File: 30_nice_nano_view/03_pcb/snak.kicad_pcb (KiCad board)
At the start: 2 copper layers, 114 x 99 mm, 114 parts

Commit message: update
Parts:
- removed the REF** at (166.2, 79.5)
- removed the REF** at (166.2, 62.0)
- removed the REF** at (197.5, 123.0)
- removed the REF** at (94.8, 84.0)
- removed the REF** at (94.8, 66.5)
- removed the REF** at (113.2, 90.2)
- removed the REF** at (113.2, 72.8)
- removed the REF** at (113.2, 55.2)
- removed the REF** at (131.8, 84.2)
- removed the REF** at (131.8, 66.8)
- removed the REF** at (131.8, 49.2)
- removed the REF** at (150.2, 91.5)
- removed the REF** at (150.2, 74.0)
- removed the REF** at (150.2, 56.5)
- removed the REF** at (168.8, 84.2)
- removed the REF** at (168.8, 66.7)
- removed the REF** at (165.2, 114.8)
- removed the REF** at (193.1, 126.1)
- removed the REF** at (100.0, 85.0)
- removed the REF** at (100.0, 67.5)
- removed the REF** at (118.5, 91.2)
- removed the REF** at (118.5, 73.8)
- removed the REF** at (118.5, 56.2)
- removed the REF** at (137.0, 85.2)
- removed the REF** at (137.0, 67.8)
- removed the REF** at (137.0, 50.2)
- removed the REF** at (155.5, 92.5)
- removed the REF** at (155.5, 75.0)
- removed the REF** at (155.5, 57.5)
- removed the REF** at (174.0, 85.2)
- removed the REF** at (174.0, 67.7)
- removed the REF** at (170.0, 117.3)
- removed the REF** at (187.9, 124.6)
- removed the REF** at (100.0, 86.0)
- removed the REF** at (100.0, 68.5)
- removed the REF** at (118.5, 92.2)
- removed the REF** at (118.5, 74.8)
- removed the REF** at (118.5, 57.2)
- removed the REF** at (137.0, 86.2)
- removed the REF** at (137.0, 68.8)
- removed the REF** at (137.0, 51.2)
- removed the REF** at (155.5, 93.5)
- removed the REF** at (155.5, 76.0)
- removed the REF** at (155.5, 58.5)
- removed the REF** at (174.0, 86.2)
- removed the REF** at (174.0, 68.7)
- removed the REF** at (169.7, 118.3)
- removed the REF** at (187.5, 125.5)
- removed the REF** at (186.9, 94.1)
- removed the REF** at (186.1, 93.4)
- removed the REF** at (185.3, 92.6)
- removed the REF** at (193.7, 94.5)
- removed the REF** at (193.2, 58.0)
- removed the REF** at (196.4, 103.4)
- removed the REF** at (202.7, 103.4)
- added REF**: VIA-0.6mm, VIA-0.6mm, F.Cu at (166.2, 78.2)
- added REF**: VIA-0.6mm, VIA-0.6mm, F.Cu at (166.2, 60.7)
- added REF**: VIA-0.6mm, VIA-0.6mm, F.Cu at (183.6, 116.0)
- added REF**: VIA-0.6mm, VIA-0.6mm, F.Cu at (93.8, 84.0)
- added REF**: VIA-0.6mm, VIA-0.6mm, F.Cu at (93.8, 66.5)
- added REF**: VIA-0.6mm, VIA-0.6mm, F.Cu at (112.2, 90.2)
- added REF**: VIA-0.6mm, VIA-0.6mm, F.Cu at (112.2, 72.8)
- added REF**: VIA-0.6mm, VIA-0.6mm, F.Cu at (112.2, 55.2)
- added REF**: VIA-0.6mm, VIA-0.6mm, F.Cu at (130.8, 84.2)
- added REF**: VIA-0.6mm, VIA-0.6mm, F.Cu at (130.8, 66.8)
- added REF**: VIA-0.6mm, VIA-0.6mm, F.Cu at (130.8, 49.2)
- added REF**: VIA-0.6mm, VIA-0.6mm, F.Cu at (149.2, 91.5)
- added REF**: VIA-0.6mm, VIA-0.6mm, F.Cu at (149.2, 74.0)
- added REF**: VIA-0.6mm, VIA-0.6mm, F.Cu at (149.2, 56.5)
- added REF**: VIA-0.6mm, VIA-0.6mm, F.Cu at (167.8, 83.0)
- added REF**: VIA-0.6mm, VIA-0.6mm, F.Cu at (167.8, 65.5)
- added REF**: VIA-0.6mm, VIA-0.6mm, F.Cu at (164.3, 114.6)
- added REF**: VIA-0.6mm, VIA-0.6mm, F.Cu at (182.8, 120.9)
- added REF**: VIA-0.6mm, VIA-0.6mm, F.Cu at (106.2, 79.2)
- added REF**: VIA-0.6mm, VIA-0.6mm, F.Cu at (106.2, 61.8)
- added REF**: VIA-0.6mm, VIA-0.6mm, F.Cu at (124.8, 85.5)
- added REF**: VIA-0.6mm, VIA-0.6mm, F.Cu at (124.8, 68.0)
- added REF**: VIA-0.6mm, VIA-0.6mm, F.Cu at (124.8, 50.5)
- added REF**: VIA-0.6mm, VIA-0.6mm, F.Cu at (143.2, 79.5)
- added REF**: VIA-0.6mm, VIA-0.6mm, F.Cu at (143.2, 62.0)
- added REF**: VIA-0.6mm, VIA-0.6mm, F.Cu at (143.2, 44.5)
- added REF**: VIA-0.6mm, VIA-0.6mm, F.Cu at (161.8, 86.7)
- added REF**: VIA-0.6mm, VIA-0.6mm, F.Cu at (161.8, 69.2)
- added REF**: VIA-0.6mm, VIA-0.6mm, F.Cu at (161.8, 51.7)
- added REF**: VIA-0.6mm, VIA-0.6mm, F.Cu at (180.2, 78.2)
- added REF**: VIA-0.6mm, VIA-0.6mm, F.Cu at (180.2, 60.7)
- added REF**: VIA-0.6mm, VIA-0.6mm, F.Cu at (177.6, 113.7)
- added REF**: VIA-0.6mm, VIA-0.6mm, F.Cu at (100.0, 85.5)
- added REF**: VIA-0.6mm, VIA-0.6mm, F.Cu at (100.0, 68.0)
- added REF**: VIA-0.6mm, VIA-0.6mm, F.Cu at (118.5, 91.8)
- added REF**: VIA-0.6mm, VIA-0.6mm, F.Cu at (118.5, 74.2)
- added REF**: VIA-0.6mm, VIA-0.6mm, F.Cu at (118.5, 56.8)
- added REF**: VIA-0.6mm, VIA-0.6mm, F.Cu at (137.0, 85.8)
- added REF**: VIA-0.6mm, VIA-0.6mm, F.Cu at (137.0, 68.2)
- added REF**: VIA-0.6mm, VIA-0.6mm, F.Cu at (137.0, 50.8)
- added REF**: VIA-0.6mm, VIA-0.6mm, F.Cu at (155.5, 93.0)
- added REF**: VIA-0.6mm, VIA-0.6mm, F.Cu at (155.5, 75.5)
- added REF**: VIA-0.6mm, VIA-0.6mm, F.Cu at (155.5, 58.0)
- added REF**: VIA-0.6mm, VIA-0.6mm, F.Cu at (174.0, 84.5)
- added REF**: VIA-0.6mm, VIA-0.6mm, F.Cu at (174.0, 67.0)
- added REF**: VIA-0.6mm, VIA-0.6mm, F.Cu at (169.8, 117.8)
- added REF**: VIA-0.6mm, VIA-0.6mm, F.Cu at (187.7, 125.1)
- added REF**: VIA-0.6mm, VIA-0.6mm, F.Cu at (186.9, 92.8)
- added REF**: VIA-0.6mm, VIA-0.6mm, F.Cu at (186.1, 92.1)
- added REF**: VIA-0.6mm, VIA-0.6mm, F.Cu at (185.3, 91.3)
- added REF**: VIA-0.6mm, VIA-0.6mm, F.Cu at (193.7, 93.2)
- added REF**: VIA-0.6mm, VIA-0.6mm, F.Cu at (193.2, 56.7)
- added REF**: VIA-0.6mm, VIA-0.6mm, F.Cu at (196.4, 102.1)
- added REF**: VIA-0.6mm, VIA-0.6mm, F.Cu at (202.7, 102.1)
- moved D15 15.5 mm to (182.3, 118.7)
- moved H3 3.28 mm to (164.8, 71.4)
- moved H1 2.50 mm to (109.2, 61.1)
- moved H2 2.50 mm to (109.2, 78.7)
- moved D12 1.29 mm to (166.2, 81.2)
- moved D13 1.29 mm to (166.2, 63.7)
- moved DISP1 1.29 mm to (193.7, 79.7)
- moved JST1 1.29 mm to (200.3, 102.1)
- moved MCU1 1.29 mm to (193.7, 74.1)
- moved S12 1.29 mm to (174.0, 81.5)
- moved S13 1.29 mm to (174.0, 64.0)
- moved SW1 1.29 mm to (193.2, 57.8)
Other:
- outline, holes or cut-outs redrawn

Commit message: update
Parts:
- removed the REF** at (166.2, 78.2)
- removed the REF** at (166.2, 60.7)
- removed the REF** at (167.8, 83.0)
- removed the REF** at (167.8, 65.5)
- removed the REF** at (180.2, 78.2)
- removed the REF** at (180.2, 60.7)
- removed the REF** at (174.0, 84.5)
- removed the REF** at (174.0, 67.0)
- removed the REF** at (186.9, 92.8)
- removed the REF** at (186.1, 92.1)
- removed the REF** at (185.3, 91.3)
- removed the REF** at (193.7, 93.2)
- removed the REF** at (193.2, 56.7)
- removed the REF** at (196.4, 102.1)
- removed the REF** at (202.7, 102.1)
- added REF**: VIA-0.6mm, VIA-0.6mm, F.Cu at (166.2, 77.2)
- added REF**: VIA-0.6mm, VIA-0.6mm, F.Cu at (166.2, 59.7)
- added REF**: VIA-0.6mm, VIA-0.6mm, F.Cu at (167.8, 82.0)
- added REF**: VIA-0.6mm, VIA-0.6mm, F.Cu at (167.8, 64.5)
- added REF**: VIA-0.6mm, VIA-0.6mm, F.Cu at (180.2, 77.2)
- added REF**: VIA-0.6mm, VIA-0.6mm, F.Cu at (180.2, 59.7)
- added REF**: VIA-0.6mm, VIA-0.6mm, F.Cu at (174.0, 83.5)
- added REF**: VIA-0.6mm, VIA-0.6mm, F.Cu at (174.0, 66.0)
- added REF**: VIA-0.6mm, VIA-0.6mm, F.Cu at (186.9, 97.4)
- added REF**: VIA-0.6mm, VIA-0.6mm, F.Cu at (186.1, 96.7)
- added REF**: VIA-0.6mm, VIA-0.6mm, F.Cu at (185.3, 95.9)
- added REF**: VIA-0.6mm, VIA-0.6mm, F.Cu at (193.7, 97.8)
- added REF**: VIA-0.6mm, VIA-0.6mm, F.Cu at (193.2, 61.3)
- added REF**: VIA-0.6mm, VIA-0.6mm, F.Cu at (194.9, 106.5)
- added REF**: VIA-0.6mm, VIA-0.6mm, F.Cu at (201.2, 106.5)
- moved JST1 4.56 mm to (198.8, 106.5)
- moved DISP1 4.55 mm to (193.7, 84.2)
- moved MCU1 4.55 mm to (193.7, 78.7)
- moved SW1 4.55 mm to (193.2, 62.4)
- moved D12 1.00 mm to (166.2, 80.2)
- moved D13 1.00 mm to (166.2, 62.7)
- moved H3 1.00 mm to (164.8, 70.4)
- moved S12 1.00 mm to (174.0, 80.5)
- moved S13 1.00 mm to (174.0, 63.0)
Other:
- outline, holes or cut-outs redrawn

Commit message: update
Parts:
- removed the REF** at (178.3, 124.1)
- removed the REF** at (193.2, 61.3)
- added H10: , mounting_hole, F.Cu at (199.9, 62.5)
- added H5: , mounting_hole, F.Cu at (155.5, 44.3)
- added H6: , mounting_hole, F.Cu at (155.5, 100.6)
- added H7: , mounting_hole, F.Cu at (169.5, 52.3)
- added H8: , mounting_hole, F.Cu at (169.5, 91.1)
- added H9: , mounting_hole, F.Cu at (176.8, 126.5)
- added REF**: VIA-0.6mm, VIA-0.6mm, F.Cu at (193.2, 60.9)
- moved H4 65.2 mm to (118.5, 99.4), turned to 0 degrees
- moved H3 53.7 mm to (118.5, 43.1)
- moved H2 15.3 mm to (104.5, 93.2)
- moved H1 8.29 mm to (104.5, 54.4)
- moved SW1 0.35 mm to (193.2, 62.1)
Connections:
- net DPC renamed SCK
- net DPD renamed MOSI
- net DPE renamed CS
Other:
- outline, holes or cut-outs redrawn

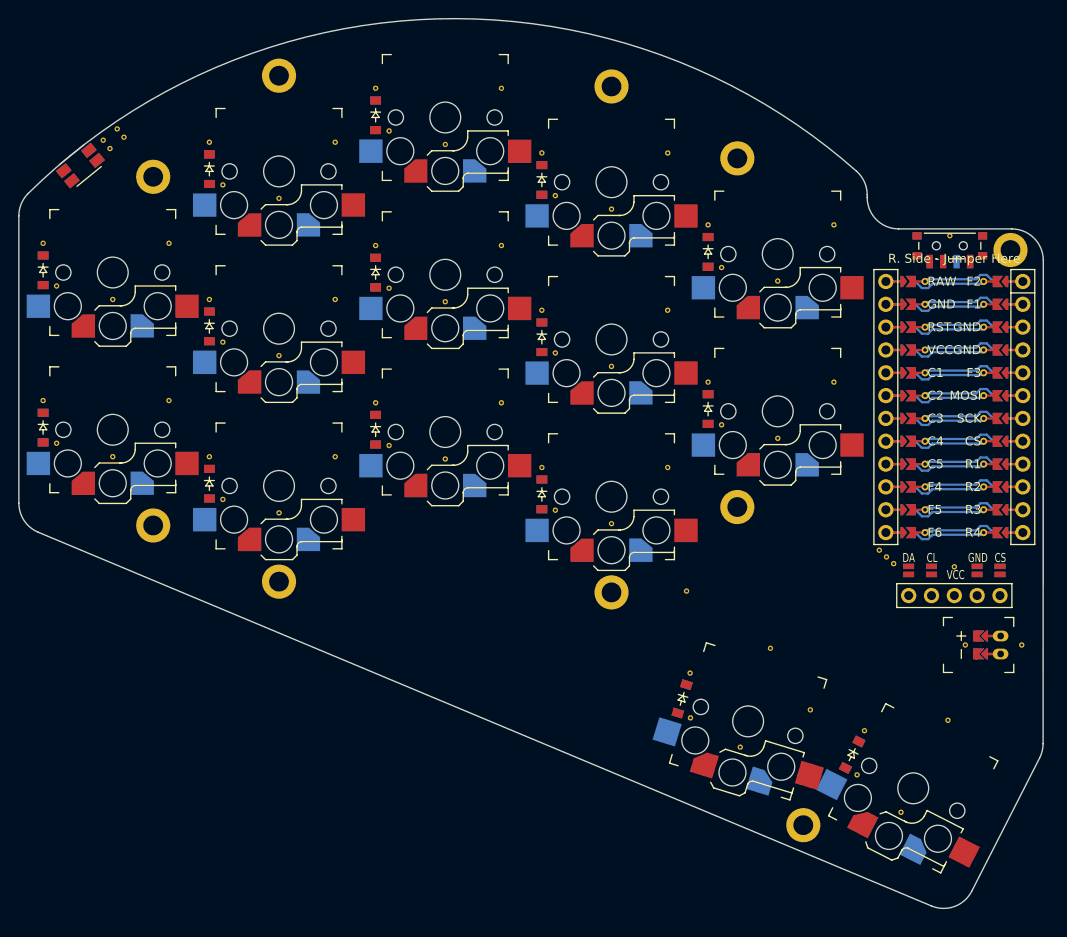
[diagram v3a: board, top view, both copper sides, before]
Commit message: add round bottom to pcb
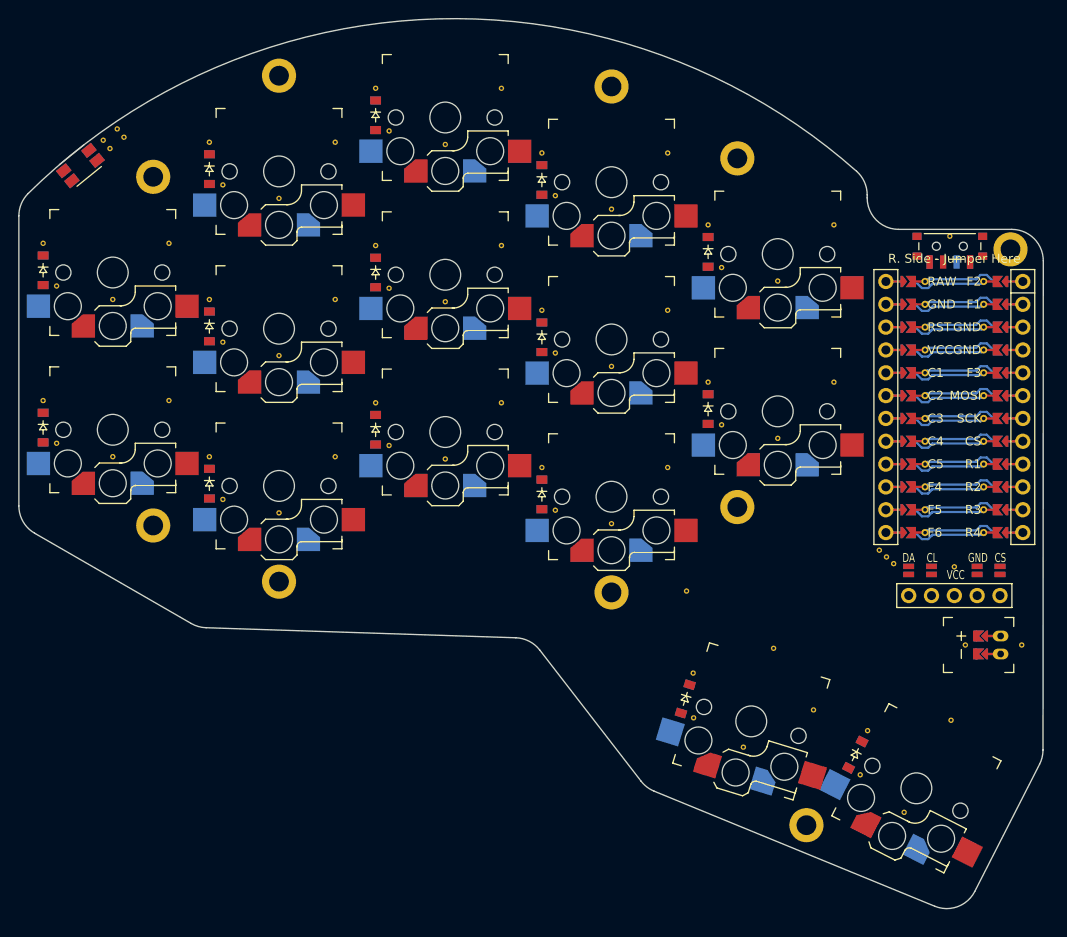
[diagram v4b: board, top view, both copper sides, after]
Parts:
- removed the REF** at (164.2, 109.6)
- removed the REF** at (183.6, 116.0)
- removed the REF** at (164.3, 114.6)
- removed the REF** at (182.8, 120.9)
- removed the REF** at (177.6, 113.7)
- removed the REF** at (169.8, 117.8)
- removed the REF** at (187.7, 125.1)
- removed the REF** at (173.2, 106.8)
- removed the REF** at (192.9, 114.8)
- removed the REF** at (193.2, 60.9)
- added REF**: VIA-0.6mm, VIA-0.6mm, F.Cu at (164.6, 109.6)
- added REF**: VIA-0.6mm, VIA-0.6mm, F.Cu at (184.0, 116.0)
- added REF**: VIA-0.6mm, VIA-0.6mm, F.Cu at (164.6, 114.6)
- added REF**: VIA-0.6mm, VIA-0.6mm, F.Cu at (183.2, 120.9)
- added REF**: VIA-0.6mm, VIA-0.6mm, F.Cu at (178.0, 113.7)
- added REF**: VIA-0.6mm, VIA-0.6mm, F.Cu at (170.2, 117.8)
- added REF**: VIA-0.6mm, VIA-0.6mm, F.Cu at (188.1, 125.1)
- added REF**: VIA-0.6mm, VIA-0.6mm, F.Cu at (173.5, 106.8)
- added REF**: VIA-0.6mm, VIA-0.6mm, F.Cu at (193.3, 114.8)
- added REF**: VIA-0.6mm, VIA-0.6mm, F.Cu at (193.2, 61.0)
- moved D14 0.35 mm to (163.7, 112.4)
- moved D15 0.35 mm to (182.6, 118.7)
- moved H9 0.35 mm to (177.2, 126.5)
- moved S14 0.35 mm to (171.1, 115.0)
- moved S15 0.35 mm to (189.4, 122.4)
- moved H10 0.07 mm to (199.9, 62.4)
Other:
- outline, holes or cut-outs redrawn

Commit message: update 30 key nicenano board
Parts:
- removed the REF** at (93.8, 84.0)
- removed the REF** at (93.8, 66.5)
- removed the REF** at (112.2, 90.2)
- removed the REF** at (112.2, 72.8)
- removed the REF** at (112.2, 55.2)
- removed the REF** at (130.8, 84.2)
- removed the REF** at (130.8, 66.8)
- removed the REF** at (130.8, 49.2)
- removed the REF** at (149.2, 91.5)
- removed the REF** at (149.2, 74.0)
- removed the REF** at (149.2, 56.5)
- removed the REF** at (167.8, 82.0)
- removed the REF** at (167.8, 64.5)
- removed the REF** at (164.6, 114.6)
- removed the REF** at (183.2, 120.9)
- removed the REF** at (106.2, 79.2)
- removed the REF** at (106.2, 61.8)
- removed the REF** at (124.8, 85.5)
- removed the REF** at (124.8, 68.0)
- removed the REF** at (124.8, 50.5)
- removed the REF** at (143.2, 79.5)
- removed the REF** at (143.2, 62.0)
- removed the REF** at (143.2, 44.5)
- removed the REF** at (161.8, 86.7)
- removed the REF** at (161.8, 69.2)
- removed the REF** at (161.8, 51.7)
- removed the REF** at (180.2, 77.2)
- removed the REF** at (180.2, 59.7)
- removed the REF** at (178.0, 113.7)
- removed the REF** at (100.0, 85.5)
- removed the REF** at (100.0, 68.0)
- removed the REF** at (118.5, 91.8)
- removed the REF** at (118.5, 74.2)
- removed the REF** at (118.5, 56.8)
- removed the REF** at (137.0, 85.8)
- removed the REF** at (137.0, 68.2)
- removed the REF** at (137.0, 50.8)
- removed the REF** at (155.5, 93.0)
- removed the REF** at (155.5, 75.5)
- removed the REF** at (155.5, 58.0)
- removed the REF** at (174.0, 83.5)
- removed the REF** at (174.0, 66.0)
- removed the REF** at (170.2, 117.8)
- removed the REF** at (188.1, 125.1)
- removed the REF** at (163.8, 100.5)
- removed the REF** at (173.5, 106.8)
- removed the REF** at (193.3, 114.8)
- removed the REF** at (194.9, 106.5)
- removed the REF** at (201.2, 106.5)
- removed the REF** at (98.9, 50.3)
- removed the REF** at (101.2, 49.9)
- removed the REF** at (99.7, 51.2)
- removed the REF** at (100.5, 49.0)
- added D16: , ceoloide:diode_tht_sod123, B.Cu at (92.2, 82.2)
- added D17: , ceoloide:diode_tht_sod123, B.Cu at (92.2, 64.8)
- added D18: , ceoloide:diode_tht_sod123, B.Cu at (110.8, 88.5)
- added D19: , ceoloide:diode_tht_sod123, B.Cu at (110.8, 71.0)
- added D20: , ceoloide:diode_tht_sod123, B.Cu at (110.8, 53.5)
- added D21: , ceoloide:diode_tht_sod123, B.Cu at (129.2, 82.5)
- added D22: , ceoloide:diode_tht_sod123, B.Cu at (129.2, 65.0)
- added D23: , ceoloide:diode_tht_sod123, B.Cu at (129.2, 47.5)
- added D24: , ceoloide:diode_tht_sod123, B.Cu at (147.8, 89.7)
- added D25: , ceoloide:diode_tht_sod123, B.Cu at (147.8, 72.2)
- added D26: , ceoloide:diode_tht_sod123, B.Cu at (147.8, 54.7)
- added D27: , ceoloide:diode_tht_sod123, B.Cu at (166.2, 80.2)
- added D28: , ceoloide:diode_tht_sod123, B.Cu at (166.2, 62.7)
- added D29: , ceoloide:diode_tht_sod123, B.Cu at (163.7, 112.4)
- added D30: , ceoloide:diode_tht_sod123, B.Cu at (182.6, 118.7)
- added REF**: VIA-0.6mm, VIA-0.6mm, F.Cu at (107.8, 79.2)
- added REF**: VIA-0.6mm, VIA-0.6mm, F.Cu at (163.2, 69.2)
- added REF**: VIA-0.6mm, VIA-0.6mm, F.Cu at (178.4, 102.6)
- added REF**: VIA-0.6mm, VIA-0.6mm, F.Cu at (93.7, 54.7)
- added REF**: VIA-0.6mm, VIA-0.6mm, F.Cu at (94.4, 55.7)
- added REF**: VIA-0.6mm, VIA-0.6mm, F.Cu at (163.2, 51.7)
- added REF**: VIA-0.6mm, VIA-0.6mm, F.Cu at (181.8, 77.2)
- added REF**: VIA-0.6mm, VIA-0.6mm, F.Cu at (181.8, 59.7)
- added REF**: VIA-0.6mm, VIA-0.6mm, F.Cu at (179.4, 114.1)
- added REF**: VIA-0.6mm, VIA-0.6mm, F.Cu at (197.8, 123.0)
- added REF**: VIA-0.6mm, VIA-0.6mm, F.Cu at (104.8, 84.0)
- added REF**: VIA-0.6mm, VIA-0.6mm, F.Cu at (104.8, 66.5)
- added REF**: VIA-0.6mm, VIA-0.6mm, F.Cu at (123.2, 90.2)
- added REF**: VIA-0.6mm, VIA-0.6mm, F.Cu at (123.2, 72.8)
- added REF**: VIA-0.6mm, VIA-0.6mm, F.Cu at (107.8, 61.8)
- added REF**: VIA-0.6mm, VIA-0.6mm, F.Cu at (123.2, 55.2)
- added REF**: VIA-0.6mm, VIA-0.6mm, F.Cu at (141.8, 84.2)
- added REF**: VIA-0.6mm, VIA-0.6mm, F.Cu at (141.8, 66.8)
- added REF**: VIA-0.6mm, VIA-0.6mm, F.Cu at (141.8, 49.2)
- added REF**: VIA-0.6mm, VIA-0.6mm, F.Cu at (160.2, 91.5)
- added REF**: VIA-0.6mm, VIA-0.6mm, F.Cu at (160.2, 74.0)
- added REF**: VIA-0.6mm, VIA-0.6mm, F.Cu at (160.2, 56.5)
- added REF**: VIA-0.6mm, VIA-0.6mm, F.Cu at (178.8, 82.0)
- added REF**: VIA-0.6mm, VIA-0.6mm, F.Cu at (178.8, 64.5)
- added REF**: VIA-0.6mm, VIA-0.6mm, F.Cu at (175.2, 117.8)
- added REF**: VIA-0.6mm, VIA-0.6mm, F.Cu at (126.2, 85.5)
- added REF**: VIA-0.6mm, VIA-0.6mm, F.Cu at (193.0, 125.9)
- added REF**: VIA-0.6mm, VIA-0.6mm, F.Cu at (126.2, 68.0)
- added REF**: VIA-0.6mm, VIA-0.6mm, F.Cu at (95.2, 84.0)
- added REF**: VIA-0.6mm, VIA-0.6mm, F.Cu at (95.2, 66.5)
- added REF**: VIA-0.6mm, VIA-0.6mm, F.Cu at (113.8, 90.2)
- added REF**: VIA-0.6mm, VIA-0.6mm, F.Cu at (113.8, 72.8)
- added REF**: VIA-0.6mm, VIA-0.6mm, F.Cu at (126.2, 50.5)
- added REF**: VIA-0.6mm, VIA-0.6mm, F.Cu at (113.8, 55.2)
- added REF**: VIA-0.6mm, VIA-0.6mm, F.Cu at (132.2, 84.2)
- added REF**: VIA-0.6mm, VIA-0.6mm, F.Cu at (132.2, 66.8)
- added REF**: VIA-0.6mm, VIA-0.6mm, F.Cu at (132.2, 49.2)
- added REF**: VIA-0.6mm, VIA-0.6mm, F.Cu at (150.8, 91.5)
- added REF**: VIA-0.6mm, VIA-0.6mm, F.Cu at (150.8, 74.0)
- added REF**: VIA-0.6mm, VIA-0.6mm, F.Cu at (150.8, 56.5)
- added REF**: VIA-0.6mm, VIA-0.6mm, F.Cu at (169.2, 82.0)
- added REF**: VIA-0.6mm, VIA-0.6mm, F.Cu at (169.2, 64.5)
- added REF**: VIA-0.6mm, VIA-0.6mm, F.Cu at (166.1, 115.0)
- added REF**: VIA-0.6mm, VIA-0.6mm, F.Cu at (144.8, 79.5)
- added REF**: VIA-0.6mm, VIA-0.6mm, F.Cu at (184.5, 121.6)
- added REF**: VIA-0.6mm, VIA-0.6mm, F.Cu at (100.0, 86.1)
- added REF**: VIA-0.6mm, VIA-0.6mm, F.Cu at (100.0, 68.6)
- added REF**: VIA-0.6mm, VIA-0.6mm, F.Cu at (118.5, 92.3)
- added REF**: VIA-0.6mm, VIA-0.6mm, F.Cu at (118.5, 74.8)
- added REF**: VIA-0.6mm, VIA-0.6mm, F.Cu at (118.5, 57.4)
- added REF**: VIA-0.6mm, VIA-0.6mm, F.Cu at (137.0, 86.3)
- added REF**: VIA-0.6mm, VIA-0.6mm, F.Cu at (137.0, 68.8)
- added REF**: VIA-0.6mm, VIA-0.6mm, F.Cu at (137.0, 51.4)
- added REF**: VIA-0.6mm, VIA-0.6mm, F.Cu at (155.5, 93.5)
- added REF**: VIA-0.6mm, VIA-0.6mm, F.Cu at (144.8, 62.0)
- added REF**: VIA-0.6mm, VIA-0.6mm, F.Cu at (155.5, 76.0)
- added REF**: VIA-0.6mm, VIA-0.6mm, F.Cu at (155.5, 58.6)
- added REF**: VIA-0.6mm, VIA-0.6mm, F.Cu at (174.0, 84.0)
- added REF**: VIA-0.6mm, VIA-0.6mm, F.Cu at (174.0, 66.5)
- added REF**: VIA-0.6mm, VIA-0.6mm, F.Cu at (170.0, 118.4)
- added REF**: VIA-0.6mm, VIA-0.6mm, F.Cu at (187.8, 125.6)
- added REF**: VIA-0.6mm, VIA-0.6mm, F.Cu at (100.0, 85.0)
- added REF**: VIA-0.6mm, VIA-0.6mm, F.Cu at (100.0, 67.5)
- added REF**: VIA-0.6mm, VIA-0.6mm, F.Cu at (118.5, 91.2)
- added REF**: VIA-0.6mm, VIA-0.6mm, F.Cu at (118.5, 73.8)
- added REF**: VIA-0.6mm, VIA-0.6mm, F.Cu at (144.8, 44.5)
- added REF**: VIA-0.6mm, VIA-0.6mm, F.Cu at (118.5, 56.2)
- added REF**: VIA-0.6mm, VIA-0.6mm, F.Cu at (137.0, 85.2)
- added REF**: VIA-0.6mm, VIA-0.6mm, F.Cu at (137.0, 67.8)
- added REF**: VIA-0.6mm, VIA-0.6mm, F.Cu at (137.0, 50.2)
- added REF**: VIA-0.6mm, VIA-0.6mm, F.Cu at (155.5, 92.5)
- added REF**: VIA-0.6mm, VIA-0.6mm, F.Cu at (155.5, 75.0)
- added REF**: VIA-0.6mm, VIA-0.6mm, F.Cu at (155.5, 57.5)
- added REF**: VIA-0.6mm, VIA-0.6mm, F.Cu at (174.0, 83.0)
- added REF**: VIA-0.6mm, VIA-0.6mm, F.Cu at (174.0, 65.5)
- added REF**: VIA-0.6mm, VIA-0.6mm, F.Cu at (170.3, 117.3)
- added REF**: VIA-0.6mm, VIA-0.6mm, F.Cu at (163.2, 86.7)
- added REF**: VIA-0.6mm, VIA-0.6mm, F.Cu at (188.3, 124.6)
- added REF**: VIA-0.6mm, VIA-0.6mm, F.Cu at (182.7, 112.6)
- added REF**: VIA-0.6mm, VIA-0.6mm, F.Cu at (165.4, 104.3)
- added REF**: VIA-0.6mm, VIA-0.6mm, F.Cu at (185.7, 111.0)
- added REF**: VIA-0.6mm, VIA-0.6mm, F.Cu at (178.4, 96.4)
- D1, D10, D11, D12, D13, D14, D15, D2, D3, D4, D5, D6, D7, D8, D9: footprint ComboDiode -> ceoloide:diode_tht_sod123
- moved JST1 21.3 mm to (178.4, 100.3), turned to 180 degrees
- moved D1 15.5 mm to (107.8, 82.2)
- moved D10 15.5 mm to (163.2, 72.2)
- moved D11 15.5 mm to (163.2, 54.7)
- moved D12 15.5 mm to (181.8, 80.2)
- moved D13 15.5 mm to (181.8, 62.7)
- moved D2 15.5 mm to (107.8, 64.8)
- moved D3 15.5 mm to (126.2, 88.5)
- moved D4 15.5 mm to (126.2, 71.0)
- moved D5 15.5 mm to (126.2, 53.5)
- moved D6 15.5 mm to (144.8, 82.5)
- moved D7 15.5 mm to (144.8, 65.0)
- moved D8 15.5 mm to (144.8, 47.5)
- moved D9 15.5 mm to (163.2, 89.7)
- moved D14 15.5 mm to (178.5, 117.0)
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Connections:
- S3 pad 1: C1 -> C2
- S6 pad 1: C2 -> C3
- S9 pad 1: C3 -> C4
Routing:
- net index_bot: track 0.00 -> 121.9 mm
- net C4: track 121.9 -> 0.00 mm
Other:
- outline, holes or cut-outs redrawn
